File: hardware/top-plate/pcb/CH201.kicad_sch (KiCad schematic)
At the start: 26 parts, among them U1 SN74LVC2T45DCUR

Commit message: fixed middle plate and added stuff to gitignore
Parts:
- removed U1: SN74LVC2T45DCUR, Package_SO:VSSOP-8_2.3x2mm_P0.5mm, symbol Logic_LevelTranslator:SN74LVC2T45DCUR
- added C6, C7, C8: 1uF, Capacitor_SMD:C_1206_3216Metric_Pad1.33x1.80mm_HandSolder, symbol Device:C
- added U1, U3: TXS0108EPW, Package_SO:TSSOP-20_4.4x6.5mm_P0.65mm, symbol Logic_LevelTranslator:TXS0108EPW
- C5: footprint PCM_Capacitor_SMD_AKL:C_0805_2012Metric_Pad1.15x1.40mm_HandSolder -> Capacitor_SMD:C_1206_3216Metric_Pad1.33x1.80mm_HandSolder
- FFC_US1, FFC_US10, FFC_US11, FFC_US12, FFC_US13, FFC_US14, FFC_US15, FFC_US16, FFC_US2, FFC_US3, FFC_US4, FFC_US5, FFC_US6, FFC_US7, FFC_US8, FFC_US9: footprint (none) -> EasyEDA:FPC-SMD_7P-P1.0_KINGHELM_KH-FG1.0-H2.0-7PIN
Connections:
- net +3.3V is gone; now on net +1V8: DMUX_INT.9 (VDD), DMUX_PROG.9 (VDD)
- net SCK_PROG is gone; now on net SPI_1V8.SCLK: DMUX_PROG.12 (SCK)
- net SI_PROG is gone; now on net SPI_1V8.MOSI: DMUX_PROG.13 (SI)
- net SO_PROG is gone; now on net SPI_1V8.MISO: DMUX_PROG.14 (SO)
- net +1V8: now also JP1.3 (B), JP2.3 (B), JP3.3 (B), JP4.3 (B), JP5.3 (B), JP6.3 (B), C7.2, U1.2 (VCCA), U3.2 (VCCA)
- net +3V3: now also C6.1, C8.1, U1.19 (VCCB), U3.19 (VCCB); no longer JP1.3 (B), JP2.3 (B), JP3.3 (B), JP4.3 (B), JP5.3 (B), JP6.3 (B)
- net DMUX_CS: no longer DMUX_INT.11 (~{CS})
- net DMUX_RST: no longer DMUX_PROG.11 (~{CS})
- net GND: now also C6.2, C7.1, C8.2, U3.11 (GND)
- net SCL: no longer FFC_US1.5 (Pin_5), FFC_US10.5 (Pin_5), FFC_US11.5 (Pin_5), FFC_US12.5 (Pin_5), FFC_US13.5 (Pin_5), FFC_US14.5 (Pin_5), FFC_US15.5 (Pin_5), FFC_US16.5 (Pin_5), FFC_US2.5 (Pin_5), FFC_US3.5 (Pin_5), FFC_US4.5 (Pin_5), FFC_US5.5 (Pin_5), FFC_US6.5 (Pin_5), FFC_US7.5 (Pin_5), FFC_US8.5 (Pin_5), FFC_US9.5 (Pin_5)
- net SDA: no longer FFC_US1.7 (Pin_7), FFC_US10.7 (Pin_7), FFC_US11.7 (Pin_7), FFC_US12.7 (Pin_7), FFC_US13.7 (Pin_7), FFC_US14.7 (Pin_7), FFC_US15.7 (Pin_7), FFC_US16.7 (Pin_7), FFC_US2.7 (Pin_7), FFC_US3.7 (Pin_7), FFC_US4.7 (Pin_7), FFC_US5.7 (Pin_7), FFC_US6.7 (Pin_7), FFC_US7.7 (Pin_7), FFC_US8.7 (Pin_7), FFC_US9.7 (Pin_7)
- net US_INT1: no longer FFC_US11.4 (Pin_4), FFC_US13.4 (Pin_4), FFC_US15.4 (Pin_4), FFC_US3.4 (Pin_4), FFC_US5.4 (Pin_4), FFC_US7.4 (Pin_4), FFC_US9.4 (Pin_4)
- net US_INT10: now also FFC_US10.4 (Pin_4)
- net US_INT11: now also FFC_US11.4 (Pin_4)
- net US_INT12: now also FFC_US12.4 (Pin_4)
- net US_INT13: now also FFC_US13.4 (Pin_4)
- net US_INT14: now also FFC_US14.4 (Pin_4)
- net US_INT15: now also FFC_US15.4 (Pin_4)
- net US_INT16: now also FFC_US16.4 (Pin_4)
- net US_INT2: no longer FFC_US10.4 (Pin_4), FFC_US12.4 (Pin_4), FFC_US14.4 (Pin_4), FFC_US16.4 (Pin_4), FFC_US4.4 (Pin_4), FFC_US6.4 (Pin_4), FFC_US8.4 (Pin_4)
- net US_INT3: now also FFC_US3.4 (Pin_4)
- net US_INT4: now also FFC_US4.4 (Pin_4)
- net US_INT5: now also FFC_US5.4 (Pin_4)
- net US_INT6: now also FFC_US6.4 (Pin_4)
- net US_INT7: now also FFC_US7.4 (Pin_4)
- net US_INT8: now also FFC_US8.4 (Pin_4)
- net US_INT9: now also FFC_US9.4 (Pin_4)
- net US_PROG1: no longer FFC_US11.6 (Pin_6), FFC_US13.6 (Pin_6), FFC_US15.6 (Pin_6), FFC_US3.6 (Pin_6), FFC_US5.6 (Pin_6), FFC_US7.6 (Pin_6), FFC_US9.6 (Pin_6)
- net US_PROG10: now also FFC_US10.6 (Pin_6)
- net US_PROG11: now also FFC_US11.6 (Pin_6)
- net US_PROG12: now also FFC_US12.6 (Pin_6)
- net US_PROG13: now also FFC_US13.6 (Pin_6)
- net US_PROG14: now also FFC_US14.6 (Pin_6)
- net US_PROG15: now also FFC_US15.6 (Pin_6)
- net US_PROG16: now also FFC_US16.6 (Pin_6)
- net US_PROG2: no longer FFC_US10.6 (Pin_6), FFC_US12.6 (Pin_6), FFC_US14.6 (Pin_6), FFC_US16.6 (Pin_6), FFC_US4.6 (Pin_6), FFC_US6.6 (Pin_6), FFC_US8.6 (Pin_6)
- net US_PROG3: now also FFC_US3.6 (Pin_6)
- net US_PROG4: now also FFC_US4.6 (Pin_6)
- net US_PROG5: now also FFC_US5.6 (Pin_6)
- net US_PROG6: now also FFC_US6.6 (Pin_6)
- net US_PROG7: now also FFC_US7.6 (Pin_6)
- net US_PROG8: now also FFC_US8.6 (Pin_6)
- net US_PROG9: now also FFC_US9.6 (Pin_6)
- net INTA_INT renamed INTMUX_INTA
- net INTA_PROG renamed PROGMUX_INTA
- net INTB_INT renamed INTMUX_INTB
- net INTB_PROG renamed PROGMUX_INTB
- net SCK_INT renamed SPI_1V8.SCLK
- net SPI_1V8.SCLK: now also U3.3 (A2)
- net SI_INT renamed SPI_1V8.MOSI
- net SPI_1V8.MOSI: now also U3.4 (A3)
- net SO_INT renamed SPI_1V8.MISO
- net SPI_1V8.MISO: now also U3.5 (A4)
- net US_RST renamed US_RST_1V8
- net US_RST_1V8: now also U3.8 (A7)
- new net I2C_1V8.SCL: FFC_US1.5 (Pin_5), FFC_US10.5 (Pin_5), FFC_US11.5 (Pin_5), FFC_US12.5 (Pin_5), FFC_US13.5 (Pin_5), FFC_US14.5 (Pin_5), FFC_US15.5 (Pin_5), FFC_US16.5 (Pin_5), FFC_US2.5 (Pin_5), FFC_US3.5 (Pin_5), FFC_US4.5 (Pin_5), FFC_US5.5 (Pin_5), FFC_US6.5 (Pin_5), FFC_US7.5 (Pin_5), FFC_US8.5 (Pin_5), FFC_US9.5 (Pin_5), U3.14 (B6), U3.7 (A6)
- new net I2C_1V8.SDA: FFC_US1.7 (Pin_7), FFC_US10.7 (Pin_7), FFC_US11.7 (Pin_7), FFC_US12.7 (Pin_7), FFC_US13.7 (Pin_7), FFC_US14.7 (Pin_7), FFC_US15.7 (Pin_7), FFC_US16.7 (Pin_7), FFC_US2.7 (Pin_7), FFC_US3.7 (Pin_7), FFC_US4.7 (Pin_7), FFC_US5.7 (Pin_7), FFC_US6.7 (Pin_7), FFC_US7.7 (Pin_7), FFC_US8.7 (Pin_7), FFC_US9.7 (Pin_7), U3.15 (B5), U3.6 (A5)
- new net SPI_1V8.SCS: DMUX_INT.11 (~{CS}), DMUX_PROG.11 (~{CS}), U3.1 (A1)
- new net SPI_3V3.MISO: U3.16 (B4)
- new net SPI_3V3.MOSI: U3.17 (B3)
- new net SPI_3V3.SCLK: U3.18 (B2)
- new net SPI_3V3.SCS: U3.20 (B1)
- new net US_RST_3V3: U3.13 (B7)
- no-connect marks 0 -> 2
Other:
- note added: "16 CH201s Uses shared I2C bus and reset pin. US_INTs and US_PROGs will be multiplexed by 2 digital multiplexers on the right."
- note removed: "16 CH201s They all share US_RST, SCL and SDA nets. US_INTs and US_PROGs will be multiplexed by 2 digital multiplexers on the right."
- note removed: "Level Shifter"
- moved on the sheet: DMUX_INT, DMUX_PROG, FFC_US1, JP1, JP2, JP3, JP4, JP5, JP6

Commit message: top plate schematic
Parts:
- renumbered U3 to LVL1, U1 to LVL2
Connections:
- net +1V8: now also LVL1.10 (OE), LVL2.10 (OE)
- net I2C_1V8.SCL: no longer LVL1.14 (B6)
- net I2C_1V8.SDA: no longer LVL1.15 (B5)
- net INTMUX_INTA: now also LVL2.20 (B1); no longer DMUX_INT.20 (INTA)
- net INTMUX_INTB: now also LVL2.18 (B2); no longer DMUX_INT.19 (INTB)
- net PROGMUX_INTA: now also LVL2.17 (B3); no longer DMUX_PROG.20 (INTA)
- net PROGMUX_INTB: now also LVL2.16 (B4); no longer DMUX_PROG.19 (INTB)
- net SCL: now also LVL1.14 (B6)
- net SDA: now also LVL1.15 (B5)
- net US_RST_1V8: now also LVL2.6 (A5); no longer LVL1.8 (A7)
- net DMUX2_RST: now reaches LVL1.12 (B8)
- net DMUX2_RST_1V8: now reaches LVL1.9 (A8)
- net DMUX2_RST_1V8: now also DMUX_PROG.18 (~{RESET})
- net INTMUX_INTA_1V8: now reaches LVL2.1 (A1)
- net INTMUX_INTA_1V8: now also DMUX_INT.20 (INTA)
- net US_RST: now reaches LVL2.15 (B5)
- net INTMUX_INTB_1V8: now reaches LVL2.3 (A2)
- net INTMUX_INTB_1V8: now also DMUX_INT.19 (INTB)
- net PROGMUX_INTA_1V8: now reaches LVL2.4 (A3)
- net PROGMUX_INTA_1V8: now also DMUX_PROG.20 (INTA)
- net PROGMUX_INTB_1V8: now reaches LVL2.5 (A4)
- net PROGMUX_INTB_1V8: now also DMUX_PROG.19 (INTB)
- net DMUX_RST renamed DMUX1_RST_1V8
- net DMUX1_RST_1V8: now also LVL1.8 (A7); no longer DMUX_PROG.18 (~{RESET})
- net SPI_3V3.MISO renamed MISO
- net SPI_3V3.MOSI renamed MOSI
- net SPI_3V3.SCLK renamed SCLK
- net SPI_3V3.SCS renamed SCS
- net US_RST_3V3 renamed DMUX1_RST
- no-connect marks 2 -> 6

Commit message: dunno
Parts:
- removed JP1: Jumper_3_Bridged23, Connector_PinHeader_1.27mm:PinHeader_1x03_P1.27mm_Vertical, symbol Jumper:Jumper_3_Bridged12
- added JP3: Jumper_3_Bridged12, Connector_PinHeader_1.27mm:PinHeader_1x03_P1.27mm_Vertical, symbol Jumper:Jumper_3_Bridged12
- C10: renamed from C8; footprint Capacitor_SMD:C_1206_3216Metric_Pad1.33x1.80mm_HandSolder -> PCM_Capacitor_SMD_AKL:C_1206_3216Metric_Pad1.33x1.80mm_HandSolder
- C7: renamed from C5; footprint Capacitor_SMD:C_1206_3216Metric_Pad1.33x1.80mm_HandSolder -> PCM_Capacitor_SMD_AKL:C_1206_3216Metric_Pad1.33x1.80mm_HandSolder
- C8: renamed from C6; footprint Capacitor_SMD:C_1206_3216Metric_Pad1.33x1.80mm_HandSolder -> PCM_Capacitor_SMD_AKL:C_1206_3216Metric_Pad1.33x1.80mm_HandSolder
- C9: renamed from C7; footprint Capacitor_SMD:C_1206_3216Metric_Pad1.33x1.80mm_HandSolder -> PCM_Capacitor_SMD_AKL:C_1206_3216Metric_Pad1.33x1.80mm_HandSolder
- renumbered DMUX_INT to DMUX1, DMUX_PROG to DMUX2, JP2 to JP1, JP3 to JP2, JP5 to JP4, JP6 to JP5, JP4 to JP6, LVL1 to LVL2, LVL2 to LVL3
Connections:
- net +1V8: now also JP6.1 (A), JP3.3 (B); no longer JP6.3 (B)
- net GND: now also JP6.3 (B), LVL3.11 (GND), JP3.1 (A); no longer JP6.1 (A)
- net at DMUX1.15 (A0): now also JP3.2 (C)
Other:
- note removed: "Sheet Pins"

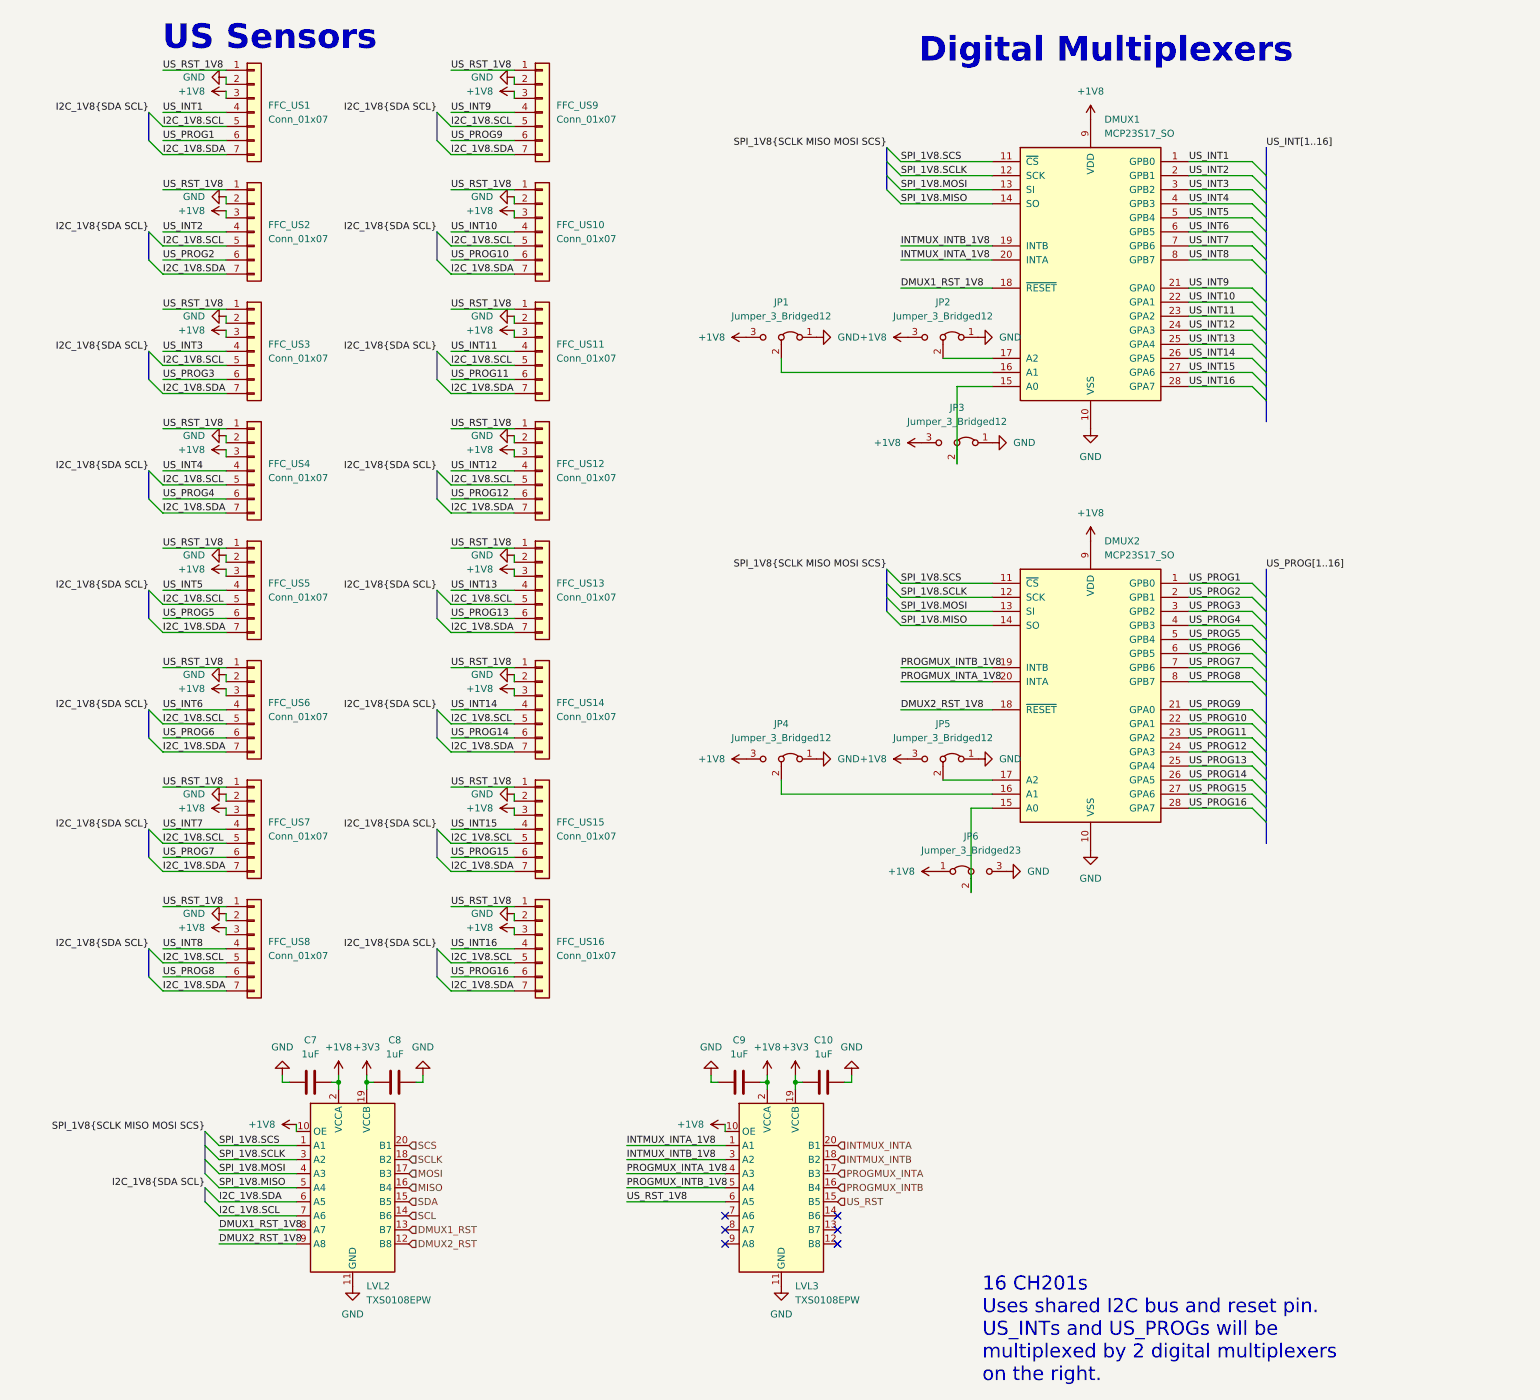
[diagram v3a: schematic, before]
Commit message: added ch201 module
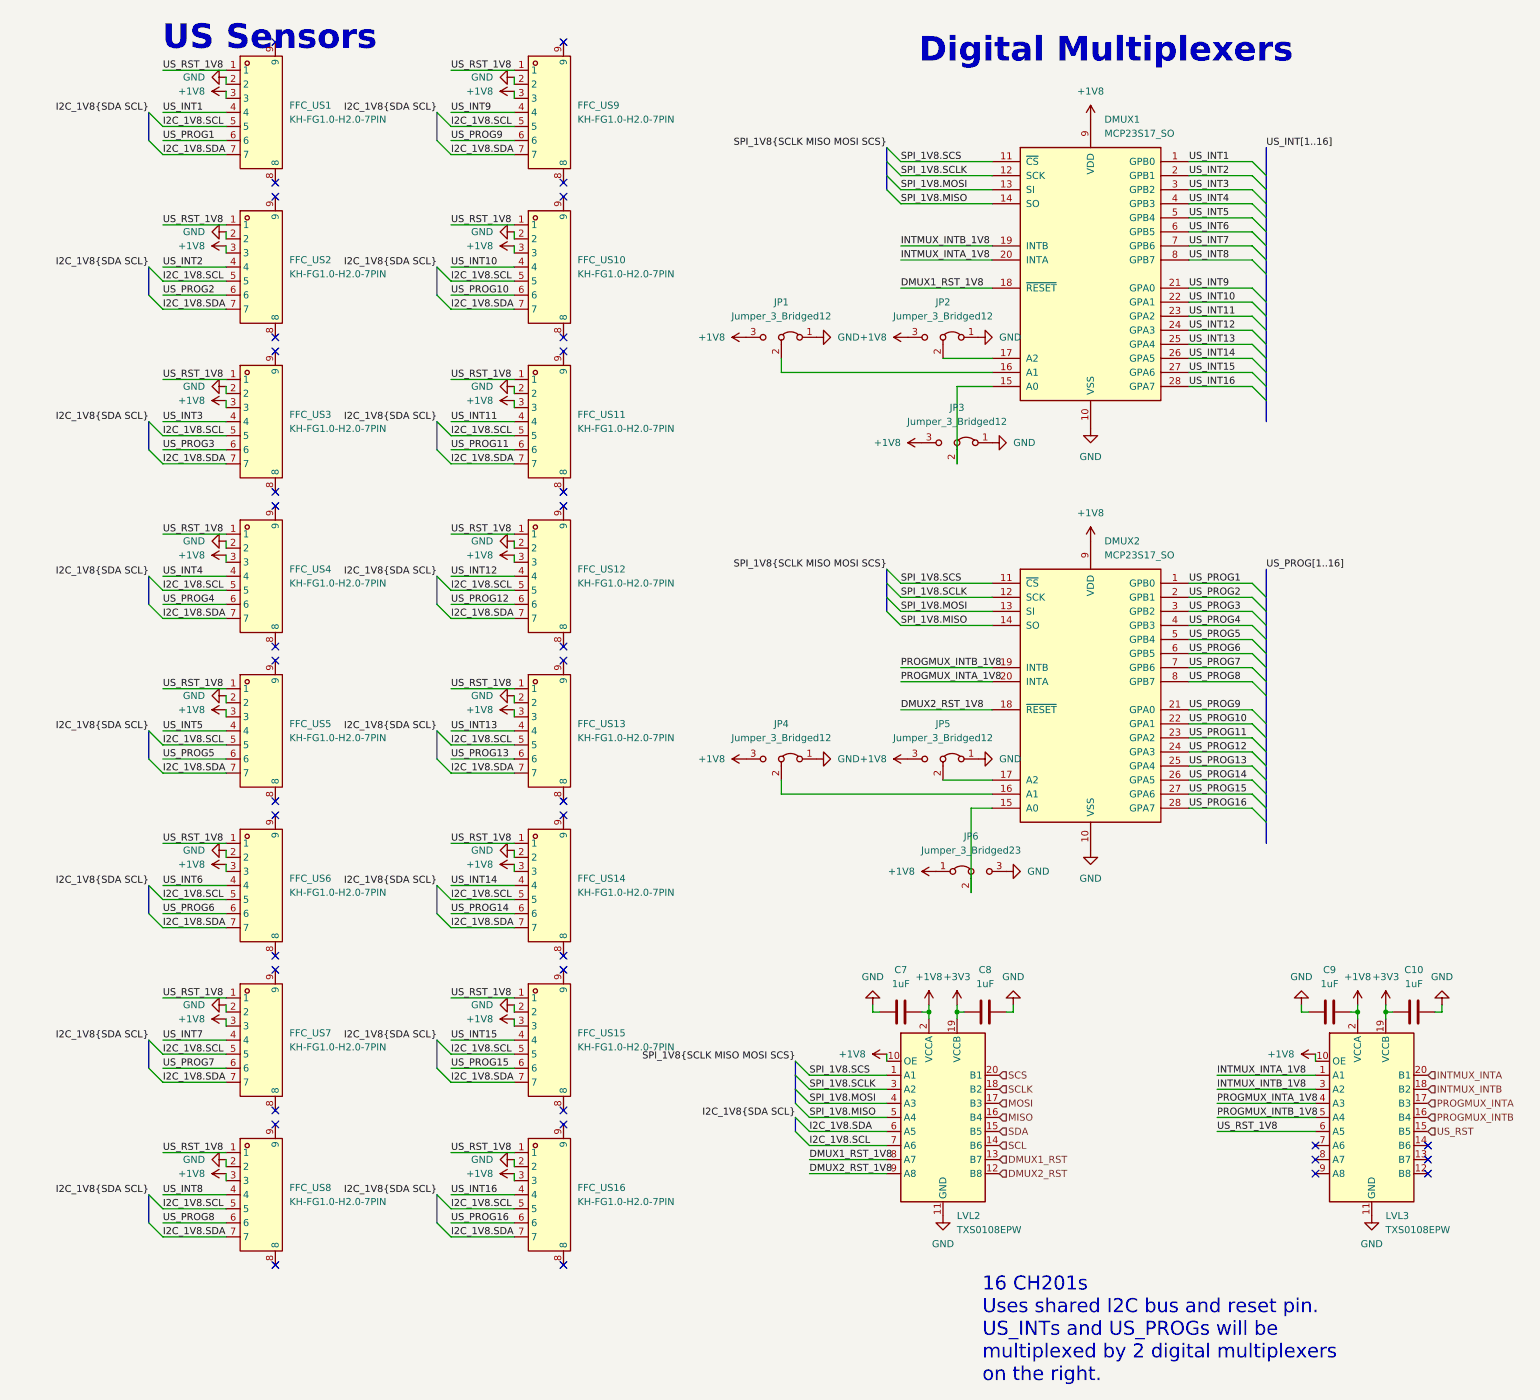
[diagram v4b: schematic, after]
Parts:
- removed FFC_US1, FFC_US10, FFC_US11, FFC_US12, FFC_US13, FFC_US14, FFC_US15, FFC_US16, FFC_US2, FFC_US3, FFC_US4, FFC_US5, FFC_US6, FFC_US7, FFC_US8, FFC_US9: Conn_01x07, EasyEDA:FPC-SMD_7P-P1.0_KINGHELM_KH-FG1.0-H2.0-7PIN, symbol Connector_Generic:Conn_01x07
- added FFC_US1, FFC_US10, FFC_US11, FFC_US12, FFC_US13, FFC_US14, FFC_US15, FFC_US16, FFC_US2, FFC_US3, FFC_US4, FFC_US5, FFC_US6, FFC_US7, FFC_US8, FFC_US9: KH-FG1.0-H2.0-7PIN, EasyEDA:FPC-SMD_7P-P1.0_KINGHELM_KH-FG1.0-H2.0-7PIN, symbol EasyEDA:KH-FG1.0-H2.0-7PIN
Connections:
- net +1V8: now also FFC_US1.3, FFC_US10.3, FFC_US11.3, FFC_US12.3, FFC_US13.3, FFC_US14.3, FFC_US15.3, FFC_US16.3, FFC_US2.3, FFC_US3.3, FFC_US4.3, FFC_US5.3, FFC_US6.3, FFC_US7.3, FFC_US8.3, FFC_US9.3
- net GND: now also FFC_US1.2, FFC_US10.2, FFC_US11.2, FFC_US12.2, FFC_US13.2, FFC_US14.2, FFC_US15.2, FFC_US16.2, FFC_US2.2, FFC_US3.2, FFC_US4.2, FFC_US5.2, FFC_US6.2, FFC_US7.2, FFC_US8.2, FFC_US9.2
- net I2C_1V8.SCL: now also FFC_US1.5, FFC_US10.5, FFC_US11.5, FFC_US12.5, FFC_US13.5, FFC_US14.5, FFC_US15.5, FFC_US16.5, FFC_US2.5, FFC_US3.5, FFC_US4.5, FFC_US5.5, FFC_US6.5, FFC_US7.5, FFC_US8.5, FFC_US9.5
- net I2C_1V8.SDA: now also FFC_US1.7, FFC_US10.7, FFC_US11.7, FFC_US12.7, FFC_US13.7, FFC_US14.7, FFC_US15.7, FFC_US16.7, FFC_US2.7, FFC_US3.7, FFC_US4.7, FFC_US5.7, FFC_US6.7, FFC_US7.7, FFC_US8.7, FFC_US9.7
- net US_INT1: now also FFC_US1.4
- net US_INT10: now also FFC_US10.4
- net US_INT11: now also FFC_US11.4
- net US_INT12: now also FFC_US12.4
- net US_INT13: now also FFC_US13.4
- net US_INT14: now also FFC_US14.4
- net US_INT15: now also FFC_US15.4
- net US_INT16: now also FFC_US16.4
- net US_INT2: now also FFC_US2.4
- net US_INT3: now also FFC_US3.4
- net US_INT4: now also FFC_US4.4
- net US_INT5: now also FFC_US5.4
- net US_INT6: now also FFC_US6.4
- net US_INT7: now also FFC_US7.4
- net US_INT8: now also FFC_US8.4
- net US_INT9: now also FFC_US9.4
- net US_PROG1: now also FFC_US1.6
- net US_PROG10: now also FFC_US10.6
- net US_PROG11: now also FFC_US11.6
- net US_PROG12: now also FFC_US12.6
- net US_PROG13: now also FFC_US13.6
- net US_PROG14: now also FFC_US14.6
- net US_PROG15: now also FFC_US15.6
- net US_PROG16: now also FFC_US16.6
- net US_PROG2: now also FFC_US2.6
- net US_PROG3: now also FFC_US3.6
- net US_PROG4: now also FFC_US4.6
- net US_PROG5: now also FFC_US5.6
- net US_PROG6: now also FFC_US6.6
- net US_PROG7: now also FFC_US7.6
- net US_PROG8: now also FFC_US8.6
- net US_PROG9: now also FFC_US9.6
- net US_RST_1V8: now also FFC_US1.1, FFC_US10.1, FFC_US11.1, FFC_US12.1, FFC_US13.1, FFC_US14.1, FFC_US15.1, FFC_US16.1, FFC_US2.1, FFC_US3.1, FFC_US4.1, FFC_US5.1, FFC_US6.1, FFC_US7.1, FFC_US8.1, FFC_US9.1
- no-connect marks 6 -> 38
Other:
- moved on the sheet: C10, C7, C8, C9, LVL2, LVL3
